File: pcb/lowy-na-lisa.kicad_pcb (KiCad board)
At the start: 2 copper layers, 29.2 x 77.9 mm, 58 parts, among them J1 Display, J3 USB_C_Receptacle_USB2.0_16P, Q1 AO3400A, Q2 AO3400A, SW1 TS24CA, SW2 TS24CA, SW3 TS24CA, SW4 TS24CA, U1 TPS61022, U2 TP4054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

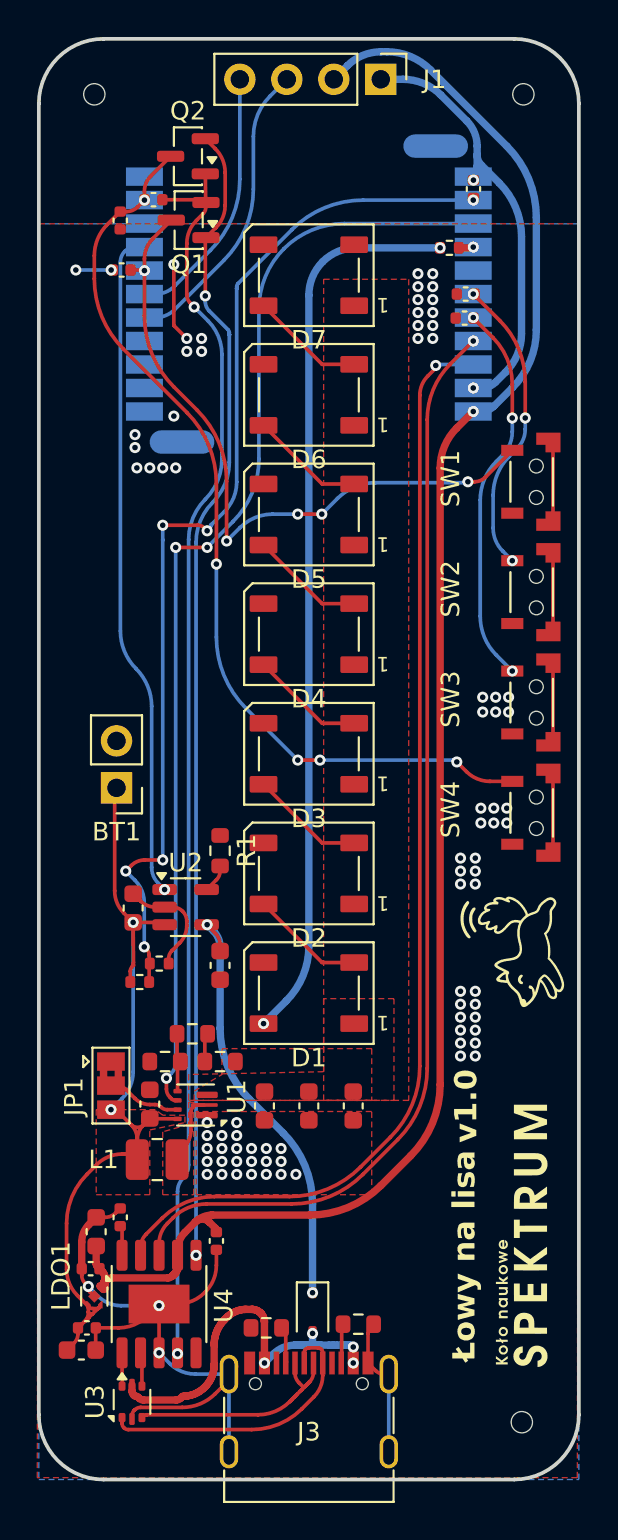
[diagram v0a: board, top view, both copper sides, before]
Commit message: pcb: rename project, final touches, cleanup
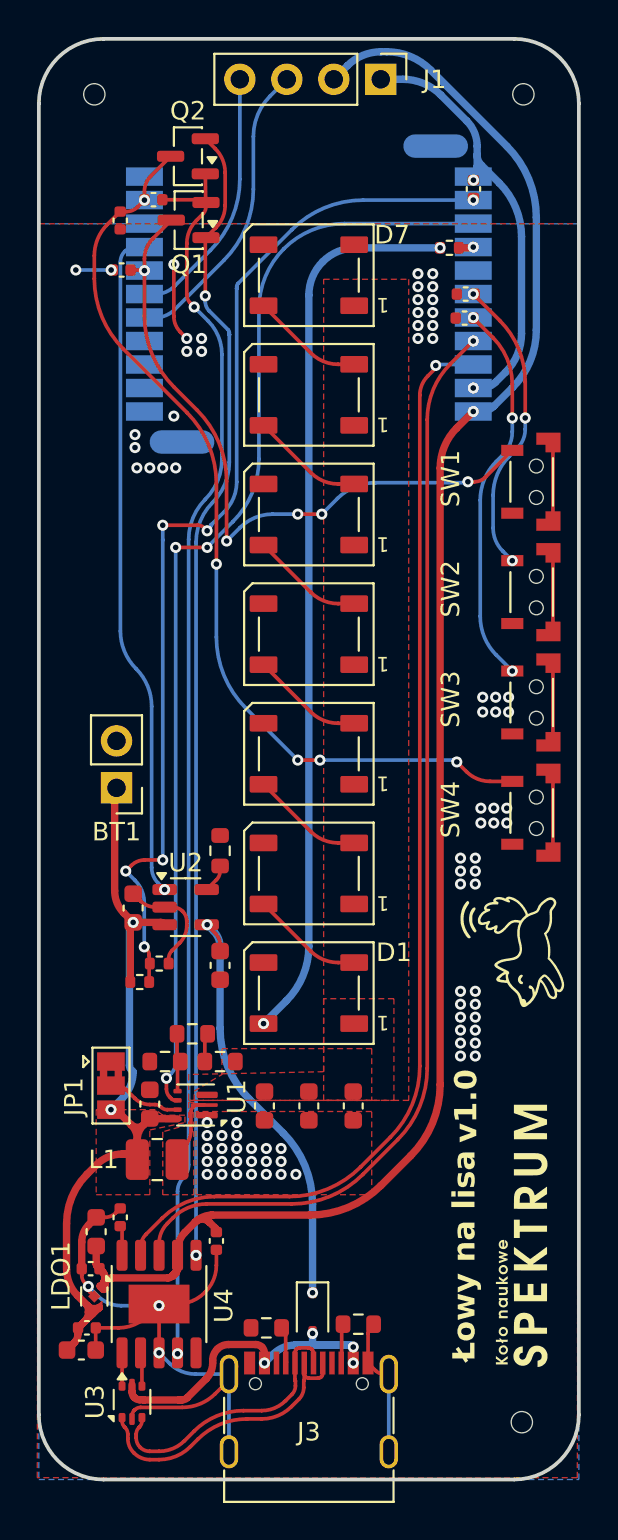
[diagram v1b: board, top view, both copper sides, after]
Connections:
- net Net-(J3-D+-PadA6) renamed C_D+
- net Net-(J3-D--PadA7) renamed C_D-
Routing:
- net 5V: track 20.7 -> 17.1 mm
- net C_D-: track 12.0 -> 15.1 mm
